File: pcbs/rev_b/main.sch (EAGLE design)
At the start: 16 parts

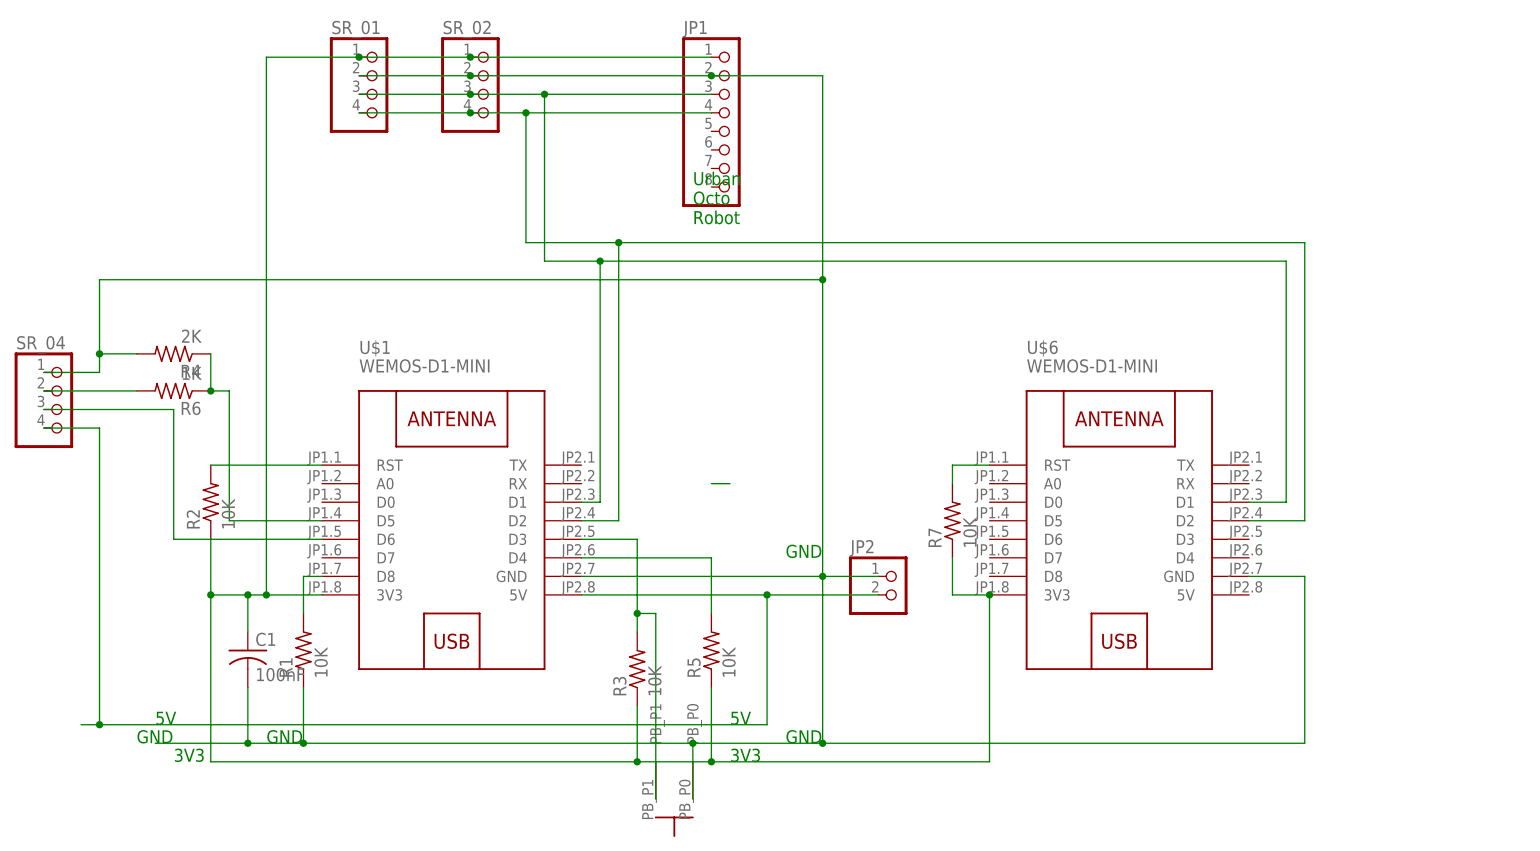
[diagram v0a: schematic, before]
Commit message: rev.b board updates - add more I2C busses for expansion - Add 5v power jumpers for expansion - Motor controller is now powered by 5v line from circuit board (less wires)
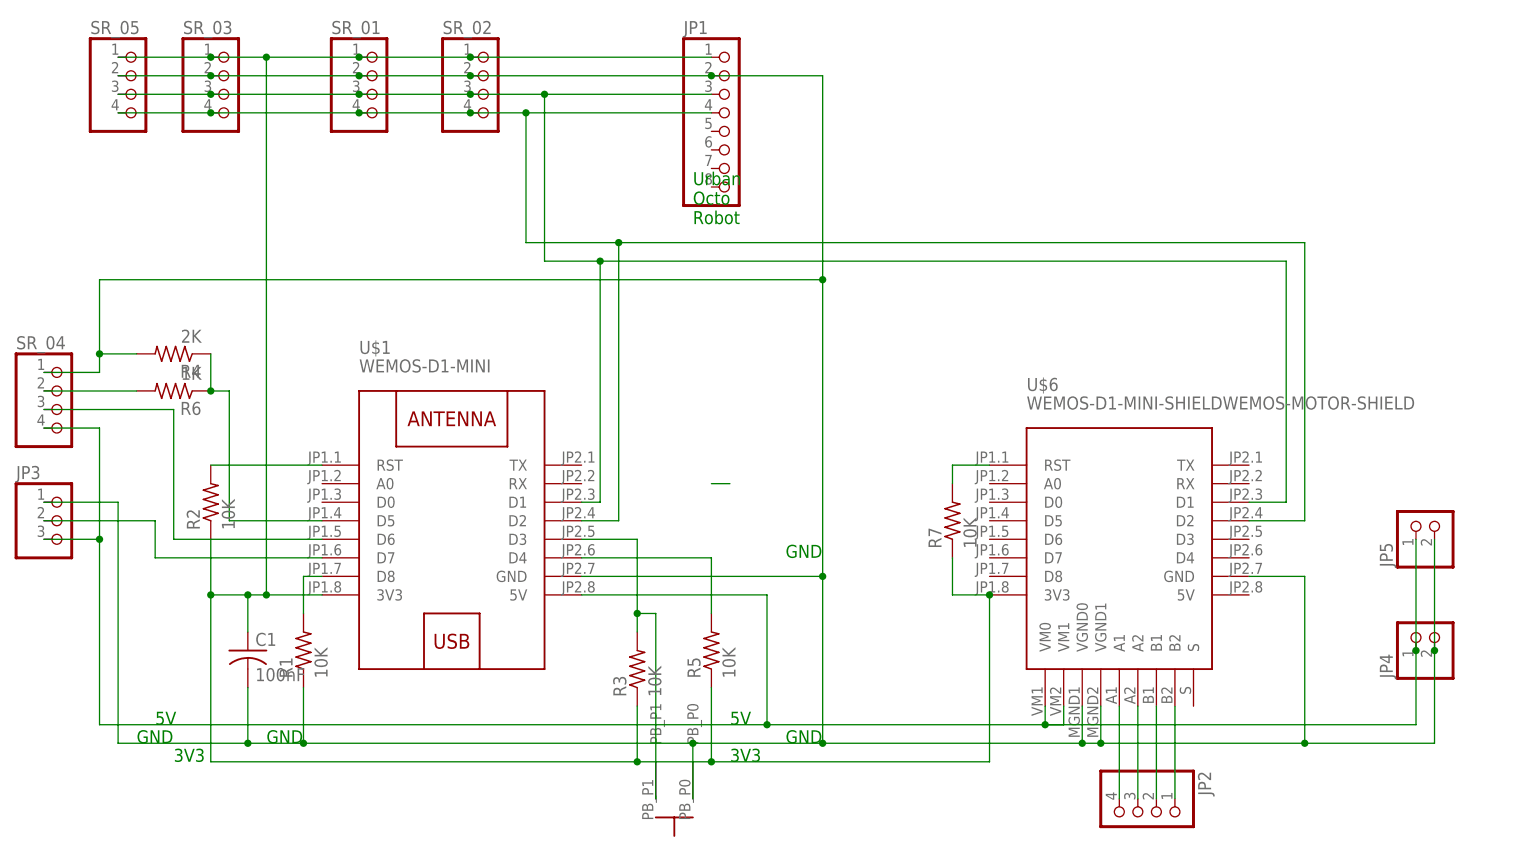
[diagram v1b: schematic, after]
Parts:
- added JP3: (no value), pinhead:PINHD-1X3
- added JP4, JP5: (no value), pinhead:PINHD-1X2
- added SR_03, SR_05: (no value), pinhead:PINHD-1X4
- JP2: device pinhead:PINHD-1X2 -> pinhead:PINHD-1X4/90
- U$6: value WEMOS-D1-MINI -> WEMOS-D1-MINI-SHIELDWEMOS-MOTOR-SHIELD; device diy-modules:WEMOS-D1-MINI -> glowmouse_custom:WEMOS-D1-MINI-SHIELDWEMOS-MOTOR-SHIELD
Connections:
- new net N$1: JP2.4, U$6.A1
- new net N$10: JP2.3, U$6.A2
- new net N$16: JP2.2, U$6.B1
- new net N$17: JP2.1, U$6.B2
- new net N$20: JP3.2, U$1.D7
- net N$2: now also JP3.1, JP4.2, JP5.2, SR_03.2, SR_05.2, U$6.VGND0, U$6.VGND1; no longer JP2.1
- net N$3: now also SR_03.3, SR_05.3
- net N$4: now also SR_03.4, SR_05.4
- net N$6: now also JP3.3, JP4.1, JP5.1, U$6.VM0, U$6.VM1; no longer JP2.2
- net N$8: now also SR_03.1, SR_05.1

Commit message: Update rev2 circuit board
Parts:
- removed SR_01, SR_02, SR_03, SR_04, SR_05: (no value), pinhead:PINHD-1X4
- added JP10, JP11, JP6, JP7, JP8, JP9: (no value), pinhead:PINHD-1X4
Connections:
- removed net N$2: C1.2, JP1.2, JP3.1, JP4.2, JP5.2, R1.1, R4.2, SR_01.2, SR_02.2, SR_03.2, SR_04.1, SR_05.2, U$1.GND, U$6.GND, U$6.VGND0, U$6.VGND1, U$7.PB_P0
- removed net N$3: JP1.3, SR_01.3, SR_02.3, SR_03.3, SR_05.3, U$1.D1, U$6.D1
- removed net N$4: JP1.4, SR_01.4, SR_02.4, SR_03.4, SR_05.4, U$1.D2, U$6.D2
- removed net N$8: C1.1, JP1.1, R2.1, R3.1, R5.1, R7.1, SR_01.1, SR_02.1, SR_03.1, SR_05.1, U$1.3V3, U$6.3V3
- new net N$19: JP7.2, U$1.D0
- new net N$21: C1.1, JP1.1, JP10.1, JP11.1, JP6.4, JP8.4, JP9.4, R2.1, R3.1, R5.1, R7.1, U$1.3V3, U$6.3V3
- new net N$22: C1.2, JP1.2, JP10.2, JP11.2, JP3.1, JP4.2, JP5.2, JP6.3, JP7.4, JP8.3, JP9.3, R1.1, R4.2, U$1.GND, U$6.GND, U$6.VGND0, U$6.VGND1, U$7.PB_P0
- new net N$23: JP1.3, JP10.3, JP11.3, JP8.2, JP9.2, U$1.D1, U$6.D1
- new net N$24: JP1.4, JP10.4, JP11.4, JP8.1, JP9.1, U$1.D2, U$6.D2
- net N$11: now also JP6.2; no longer SR_04.3
- net N$15: now also JP3.2
- net N$20: now also JP6.1; no longer JP3.2
- net N$6: now also JP7.1; no longer SR_04.4
- net N$9: now also JP7.3; no longer SR_04.2
